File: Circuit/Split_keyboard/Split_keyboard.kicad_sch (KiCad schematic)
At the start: 53 parts, among them SW1 SW_Push, SW10 SW_Push, SW11 SW_Push, SW12 SW_Push, SW13 SW_Push, SW14 SW_Push, SW15 SW_Push, SW16 SW_Push, SW17 SW_Push, SW18 SW_Push, SW19 SW_Push, SW2 SW_Push, SW20 SW_Push, SW21 SW_Push, SW22 SW_Push, SW23 SW_Push, SW24 SW_Push, SW25 SW_Push, SW26 SW_Push, SW3 SW_Push, SW4 SW_Push, SW5 SW_Push, SW6 SW_Push, SW7 SW_Push, SW8 SW_Push, SW9 SW_Push, U1 XIAO-nRF52840-SMD

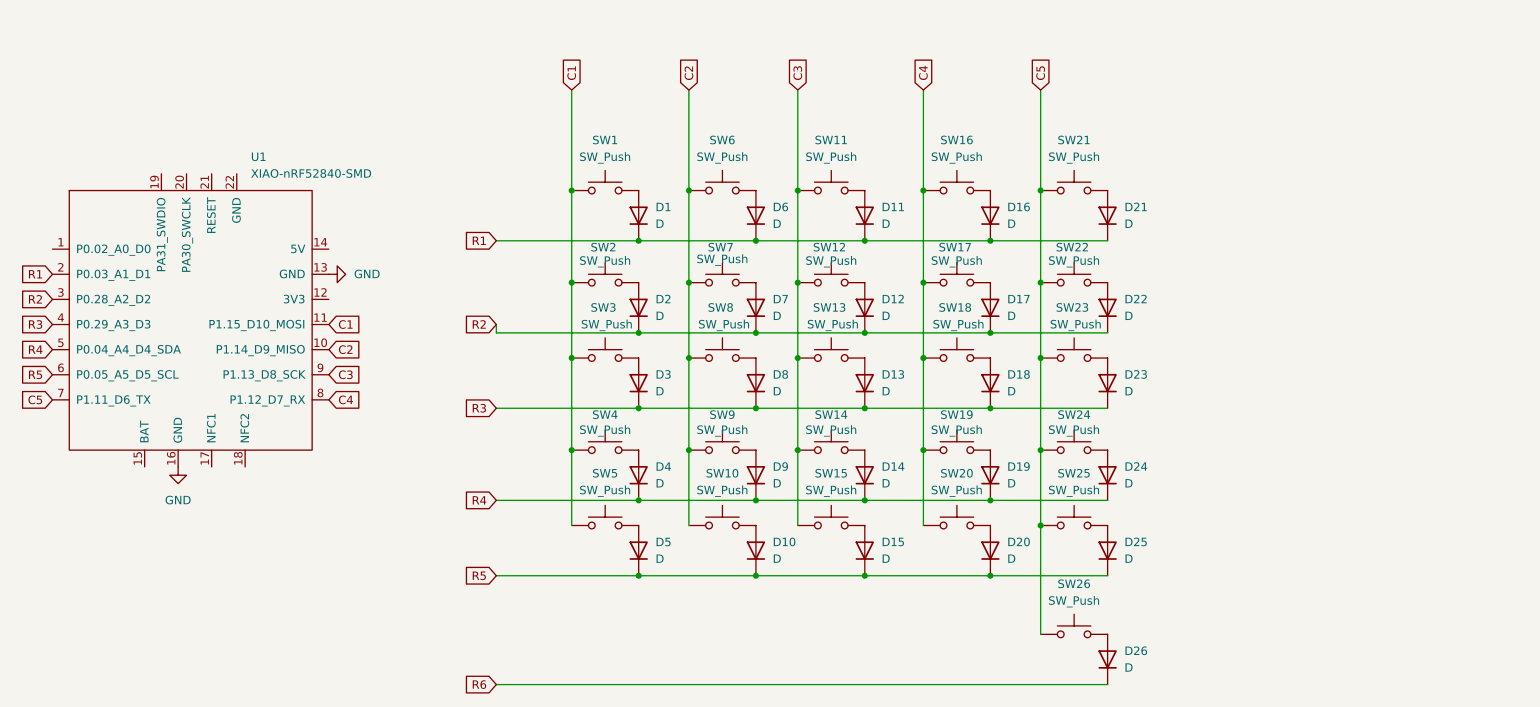
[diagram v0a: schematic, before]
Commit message: Assigned footprints and imported them into the footprint editor
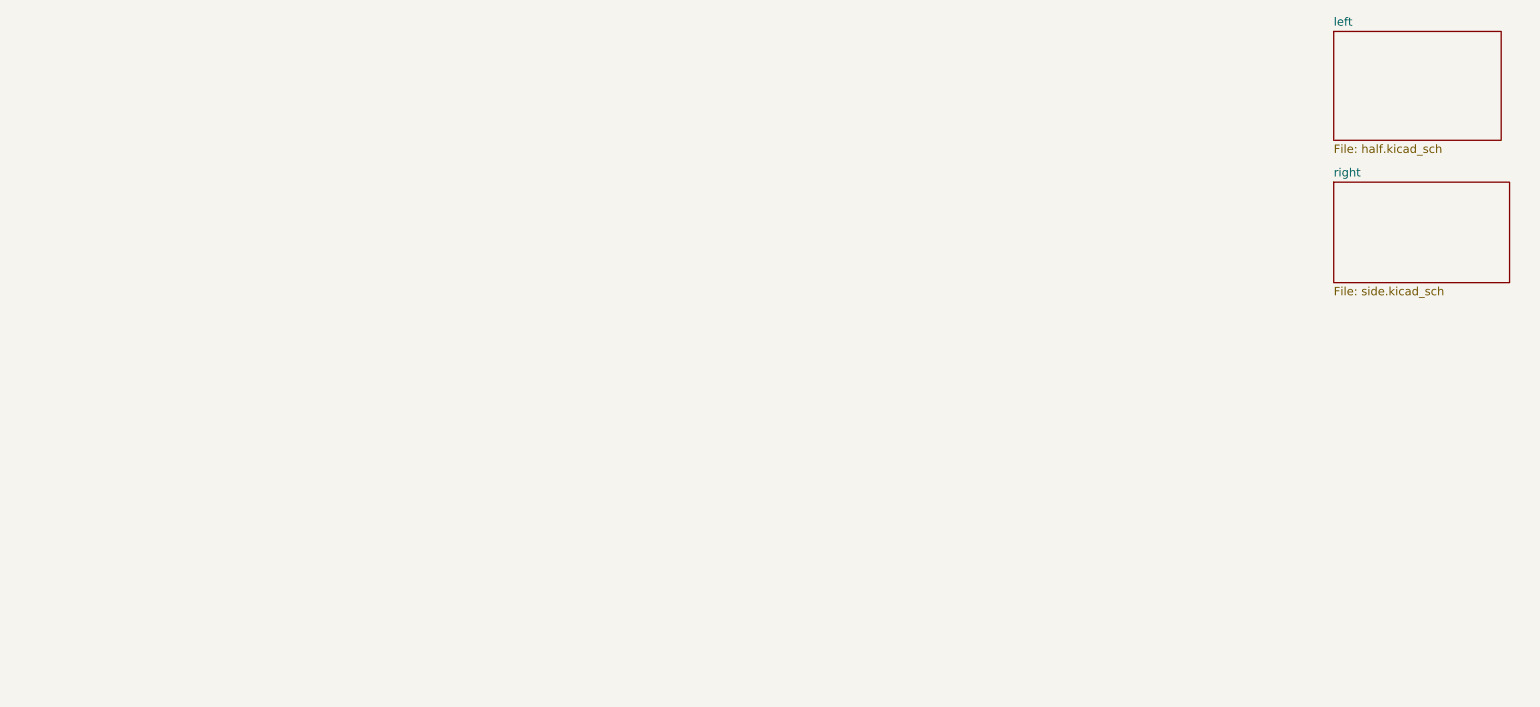
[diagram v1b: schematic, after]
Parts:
- removed D1, D10, D11, D12, D13, D14, D15, D16, D17, D18, D19, D2, D20, D21, D22, D23, D24, D25, D26, D3, D4, D5, D6, D7, D8, D9: D, symbol Device:D
- removed SW1, SW10, SW11, SW12, SW13, SW14, SW15, SW16, SW17, SW18, SW19, SW2, SW20, SW21, SW22, SW23, SW24, SW25, SW26, SW3, SW4, SW5, SW6, SW7, SW8, SW9: SW_Push, symbol Switch:SW_Push
- removed U1: XIAO-nRF52840-SMD, symbol Seeed_Studio_XIAO_Series:XIAO-nRF52840-SMD
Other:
- added sheet left (half.kicad_sch)
- added sheet right (side.kicad_sch)

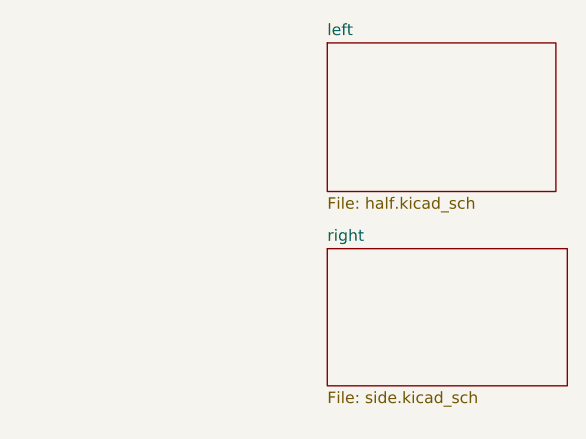
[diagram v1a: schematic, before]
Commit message: Changed the design of the footprints and maded it simliar to keeb.io keyboards
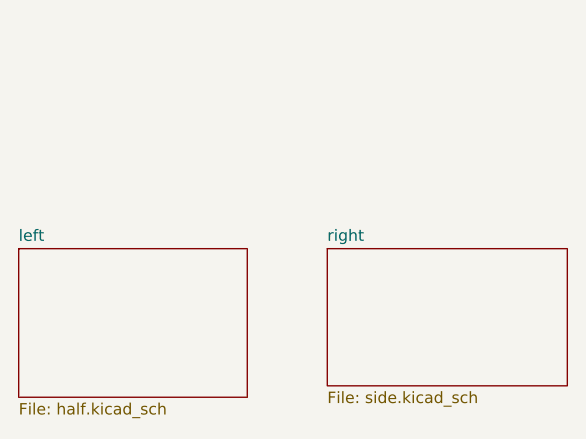
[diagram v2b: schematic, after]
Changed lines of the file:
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@@
 	)
 	(sheet
-		(at 219.71 46.99)
+		(at 185.42 69.85)
 		(size 25.4 16.51)
 		(exclude_from_sim no)
@@
 		)
 		(property "Sheetname" "left"
-			(at 219.71 46.2784 0)
+			(at 185.42 69.1384 0)
 			(effects
 				(font
@@
 		)
 		(property "Sheetfile" "half.kicad_sch"
-			(at 219.71 64.0846 0)
+			(at 185.42 86.9446 0)
 			(effects
 				(font

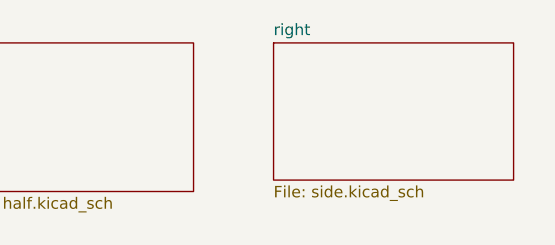
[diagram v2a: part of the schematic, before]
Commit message: Added right side and added edge.cuts for the pcb on both sides
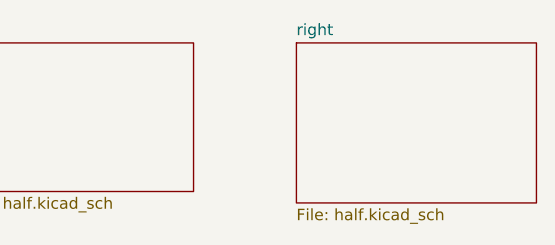
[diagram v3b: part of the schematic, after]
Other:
- sheet right: file side.kicad_sch -> half.kicad_sch
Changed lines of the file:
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@@
 	(paper "A4")
-	(sheet
-		(at 219.71 69.85)
-		(size 26.67 15.24)
-		(exclude_from_sim no)
-		(in_bom yes)
-		(on_board yes)
-		(dnp no)
-		(fields_autoplaced yes)
-		(stroke
-			(width 0.1524)
-			(type solid)
-		)
-		(fill
-			(color 0 0 0 0.0000)
-		)
-		(property "Sheetname" "right"
-			(at 219.71 69.1384 0)
-			(effects
-				(font
-					(size 1.27 1.27)
-				)
-				(justify left bottom)
-			)
-		)
-		(property "Sheetfile" "side.kicad_sch"
-			(at 219.71 85.6746 0)
-			(effects
-				(font
-					(size 1.27 1.27)
-				)
-				(justify left top)
-			)
-		)
-		(instances
-			(project "Split_keyboard"
-				(path "/746a5aca-25fe-4581-b9dd-fba448d4b64a"
-					(page "4")
-				)
-			)
-		)
-	)
 	(sheet
 		(at 185.42 69.85)
@@
 				)
 			)
+		)
+	)
+	(sheet
+		(at 222.25 69.85)
+		(size 26.67 17.78)
+		(exclude_from_sim no)
+		(in_bom yes)
+		(on_board yes)
+		(dnp no)
+		(fields_autoplaced yes)
+		(stroke
+			(width 0.1524)
+			(type solid)
+		)
+		(fill
+			(color 0 0 0 0.0000)
+		)
+		(property "Sheetname" "right"
+			(at 222.25 69.1384 0)
+			(effects
+				(font
+					(size 1.27 1.27)
+				)
+				(justify left bottom)
+			)
+		)
+		(property "Sheetfile" "half.kicad_sch"
+			(at 222.25 88.2146 0)
+			(effects
+				(font
+					(size 1.27 1.27)
+				)
+				(justify left top)
+			)
+		)
+		(instances
+			(project "Split_keyboard"
+				(path "/746a5aca-25fe-4581-b9dd-fba448d4b64a"
+					(page "3")
+				)
+			)

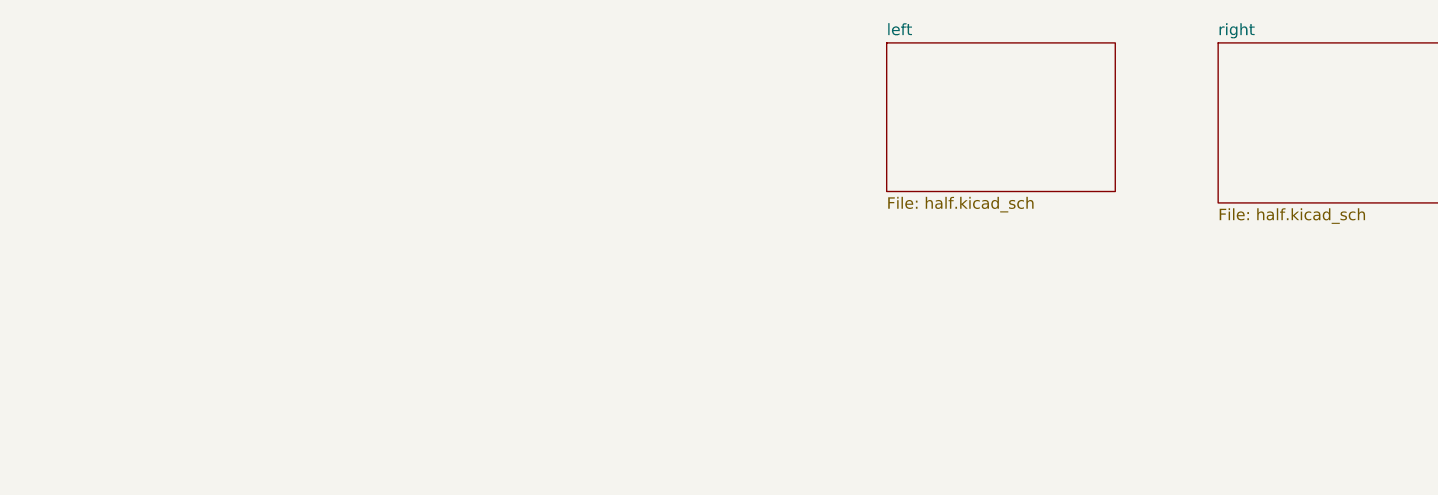
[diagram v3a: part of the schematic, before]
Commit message: Changed the design of the keyboard completelty with schematis
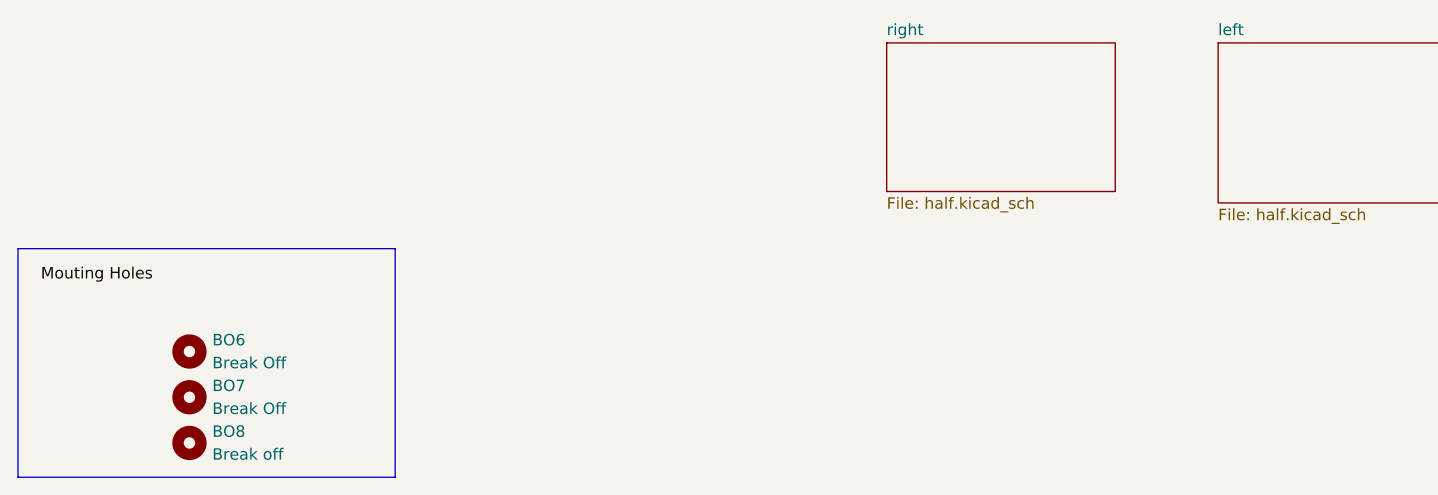
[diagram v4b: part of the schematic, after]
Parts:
- added BO6, BO7: Break Off, Panelization.pretty-master:mouse-bite-5mm-slot, symbol Mechanical:MountingHole
- added BO8: Break off, Panelization.pretty-master:mouse-bite-5mm-slot, symbol Mechanical:MountingHole
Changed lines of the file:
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@@
 	(generator_version "9.0")
 	(paper "A4")
+	(rectangle
+		(start 88.9 92.71)
+		(end 130.81 118.11)
+		(stroke
+			(width 0)
+			(type default)
+		)
+		(fill
+			(type none)
+		)
+	)
+	(label "Mouting Holes"
+		(at 91.44 96.52 0)
+		(effects
+			(font
+				(size 1.27 1.27)
+				(color 0 0 255 1)
+			)
+			(justify left bottom)
+		)
+	)
+	(symbol
+		(lib_id "Mechanical:MountingHole")
+		(at 107.95 104.14 0)
+		(unit 1)
+		(exclude_from_sim no)
+		(in_bom no)
+		(on_board yes)
+		(dnp no)
+		(property "Reference" "BO6"
+			(at 110.49 102.8699 0)
+			(effects
+				(font
+					(size 1.27 1.27)
+				)
+				(justify left)
+			)
+		)
+		(property "Value" "Break Off"
+			(at 110.49 105.4099 0)
+			(effects
+				(font
+					(size 1.27 1.27)
+				)
+				(justify left)
+			)
+		)
+		(property "Footprint" "Panelization.pretty-master:mouse-bite-5mm-slot"
+			(at 107.95 104.14 0)
+			(effects
+				(font
+					(size 1.27 1.27)
+				)
+				(hide yes)
+			)
+		)
+		(property "Datasheet" "~"
+			(at 107.95 104.14 0)
+			(effects
+				(font
+					(size 1.27 1.27)
+				)
+				(hide yes)
+			)
+		)
+		(property "Description" "Mounting Hole without connection"
+			(at 107.95 104.14 0)
+			(effects
+				(font
+					(size 1.27 1.27)
+				)
+				(hide yes)
+			)
+		)
+		(instances
+			(project "Split_keyboard"
+				(path "/746a5aca-25fe-4581-b9dd-fba448d4b64a"
+					(reference "BO6")
+					(unit 1)
+				)
+			)
+		)
+	)
+	(symbol
+		(lib_id "Mechanical:MountingHole")
+		(at 107.95 114.3 0)
+		(unit 1)
+		(exclude_from_sim no)
+		(in_bom no)
+		(on_board yes)
+		(dnp no)
+		(property "Reference" "BO8"
+			(at 110.49 113.0299 0)
+			(effects
+				(font
+					(size 1.27 1.27)
+				)
+				(justify left)
+			)
+		)
+		(property "Value" "Break off"
+			(at 110.49 115.5699 0)
+			(effects
+				(font
+					(size 1.27 1.27)
+				)
+				(justify left)
+			)
+		)
+		(property "Footprint" "Panelization.pretty-master:mouse-bite-5mm-slot"
+			(at 107.95 114.3 0)
+			(effects
+				(font
+					(size 1.27 1.27)
+				)
+				(hide yes)
+			)
+		)
+		(property "Datasheet" "~"
+			(at 107.95 114.3 0)
+			(effects
+				(font
+					(size 1.27 1.27)
+				)
+				(hide yes)
+			)
+		)
+		(property "Description" "Mounting Hole without connection"
+			(at 107.95 114.3 0)
+			(effects
+				(font
+					(size 1.27 1.27)
+				)
+				(hide yes)
+			)
+		)
+		(instances
+			(project "Split_keyboard"
+				(path "/746a5aca-25fe-4581-b9dd-fba448d4b64a"
+					(reference "BO8")
+					(unit 1)
+				)
+			)
+		)
+	)
+	(symbol
+		(lib_id "Mechanical:MountingHole")
+		(at 107.95 109.22 0)
+		(unit 1)
+		(exclude_from_sim no)
+		(in_bom no)
+		(on_board yes)
+		(dnp no)
+		(property "Reference" "BO7"
+			(at 110.49 107.9499 0)
+			(effects
+				(font
+					(size 1.27 1.27)
+				)
+				(justify left)
+			)
+		)
+		(property "Value" "Break Off"
+			(at 110.49 110.4899 0)
+			(effects
+				(font
+					(size 1.27 1.27)
+				)
+				(justify left)
+			)
+		)
+		(property "Footprint" "Panelization.pretty-master:mouse-bite-5mm-slot"
+			(at 107.95 109.22 0)
+			(effects
+				(font
+					(size 1.27 1.27)
+				)
+				(hide yes)
+			)
+		)
+		(property "Datasheet" "~"
+			(at 107.95 109.22 0)
+			(effects
+				(font
+					(size 1.27 1.27)
+				)
+				(hide yes)
+			)
+		)
+		(property "Description" "Mounting Hole without connection"
+			(at 107.95 109.22 0)
+			(effects
+				(font
+					(size 1.27 1.27)
+				)
+				(hide yes)
+			)
+		)
+		(instances
+			(project "Split_keyboard"
+				(path "/746a5aca-25fe-4581-b9dd-fba448d4b64a"
+					(reference "BO7")
+					(unit 1)
+				)
+			)
+		)
+	)
 	(sheet
 		(at 185.42 69.85)
@@
 			(color 0 0 0 0.0000)
 		)
-		(property "Sheetname" "left"
+		(property "Sheetname" "right"
 			(at 185.42 69.1384 0)
 			(effects
@@
 			(color 0 0 0 0.0000)
 		)
-		(property "Sheetname" "right"
+		(property "Sheetname" "left"
 			(at 222.25 69.1384 0)
 			(effects
